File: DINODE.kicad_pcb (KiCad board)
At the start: 2 copper layers, 29 parts, among them J1 Barrel_Jack, J10 Conn_01x03_Male, J11 Conn_02x04_Odd_Even, J2 Conn_01x02_Male, J3 Conn_01x07, J4 Conn_01x16, J5 Conn_02x04_Odd_Even, J6 Conn_02x04_Odd_Even, J7 Conn_02x04_Odd_Even, J9 Conn_02x04_Odd_Even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

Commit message: Updated design
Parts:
- added J8: AVR-ISP-6, Connector_IDC:IDC-Header_2x03_P2.54mm_Horizontal, F.Cu at (141.6, 115.6)
- RV1, RV2: footprint Potentiometer_THT:Potentiometer_Piher_PT-15-V02_Vertical -> Potentiometer_THT:Potentiometer_Piher_PT-6-V_Vertical
- SW1: footprint Button_Switch_THT:SW_PUSH-12mm -> Button_Switch_THT:SW_PUSH_6mm_H5mm
- moved J5 95.6 mm to (102.9, 121.9), turned to 270 degrees
- moved C4 74.0 mm to (114.3, 62.2), turned to 270 degrees
- moved C3 70.8 mm to (105.4, 62.2), turned to 270 degrees
- moved J3 67.9 mm to (109.2, 121.3), turned to 90 degrees
- moved U2 66.9 mm to (123.2, 85.1)
- moved U3 64.4 mm to (124.5, 55.2)
- moved D1 61.0 mm to (128.3, 64.8)
- moved R1 61.0 mm to (114.9, 114.3), turned to 180 degrees
- moved RV1 60.9 mm to (101.0, 106.7)
- moved U1 60.1 mm to (108.0, 53.3)
- moved J10 59.0 mm to (135.9, 57.8), turned to 180 degrees
- moved J4 57.1 mm to (95.2, 106.7), turned to 180 degrees
- moved R2 55.4 mm to (104.1, 114.3), turned to 180 degrees
- moved J1 54.3 mm to (100.3, 53.3)
- moved J2 50.6 mm to (142.9, 56.5), turned to 180 degrees
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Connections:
- C4 pad 1: RESET -> +5V
- C6 pad 1: RESET -> +5V
- D1 pad 2: RESET -> +5V
- D2 pad 2: PC_7 -> PD_5
- J10 pad 3: RESET -> +5V
- J2 pad 2: RESET -> +5V
- J3 pad 1: RESET -> +5V
- J4 pad 15: RESET -> +5V
- J4 pad 2: RESET -> +5V
- J5 pad 1: ESP_RX -> GND
- J5 pad 2: +3V3 -> PD_0
- J5 pad 4: Net-(J5-Pad4) -> +3V3
- J5 pad 6: +3V3 -> Net-(J5-Pad6)
- J5 pad 7: GND -> ESP_RX
- J5 pad 8: PD_0 -> +3V3
- RV1 pad 3: RESET -> +5V
- RV2 pad 3: RESET -> +5V
- SW1 pad 2: RESET -> Net-(SW1-Pad2)
- U1 pad 3: RESET -> +5V
- U2 pad 17: RESET -> +5V
- U2 pad 38: RESET -> +5V
- U2 pad 4: RESET -> Net-(SW1-Pad2)
- U2 pad 5: RESET -> +5V
- U3 pad 3: RESET -> +5V
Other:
- board text added: "BY: Jack McLeans"
- board text added: "DINODE-AVR"
- board text added: "ESP8266"
- board text added: "GSM SIM800L V2.0"
- board text added: "LCD"
- board text added: "PA0"
- board text added: "PA1"
- board text added: "PA2"
- board text added: "PA3"
- board text added: "PA4"
- board text added: "PA5"
- board text added: "PA6"
- board text added: "PA7"
- board text added: "PB0"
- board text added: "PB1"
- board text added: "PB2"
- board text added: "PB3"
- board text added: "PB4"
- board text added: "PB5"
- board text added: "PB6"
- board text added: "PB7"
- board text added: "PC0"
- board text added: "PC1"
- board text added: "PC2"
- board text added: "PC3"
- board text added: "PC4"
- board text added: "PC5"
- board text added: "PC6"
- board text added: "PC7"
- board text added: "PD0"
- board text added: "PD1"
- board text added: "PD2"
- board text added: "PD3"
- board text added: "PD4"
- board text added: "PD5"
- board text added: "PD6"
- board text added: "PD7"

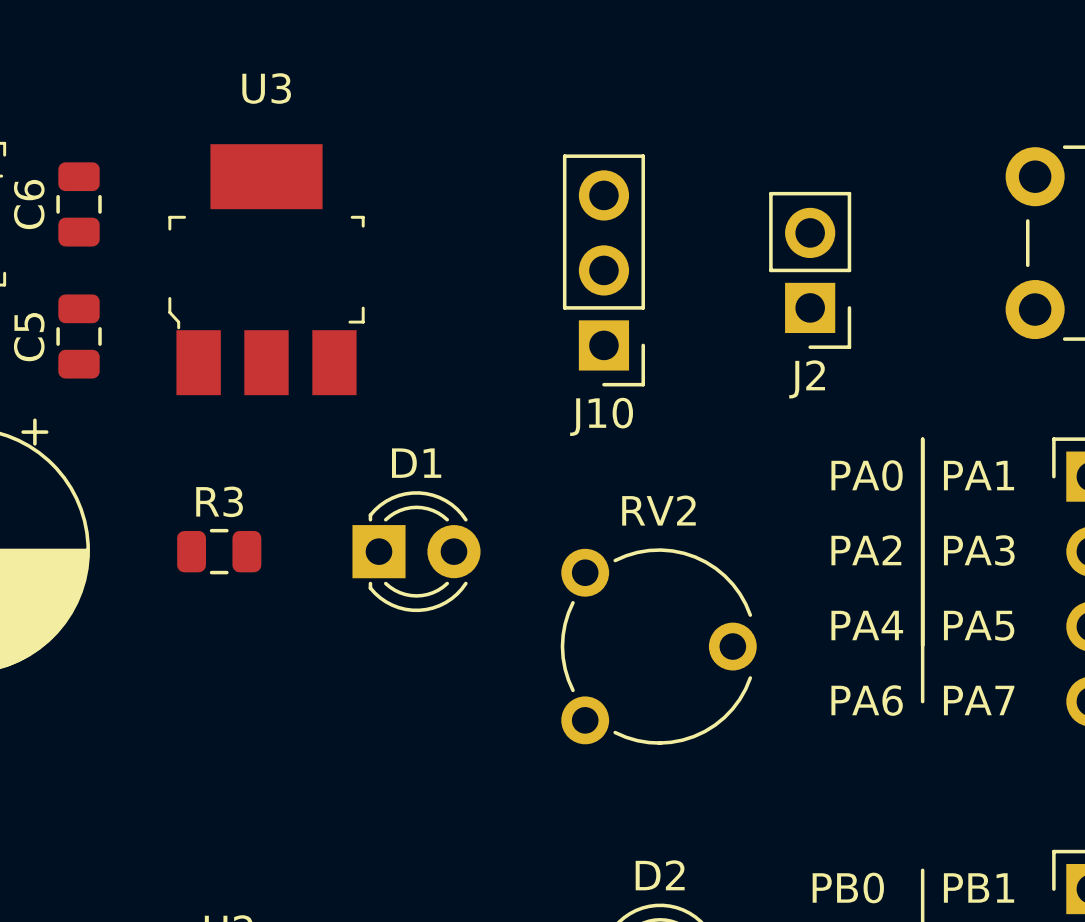
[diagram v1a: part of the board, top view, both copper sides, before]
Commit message: Updated power led position
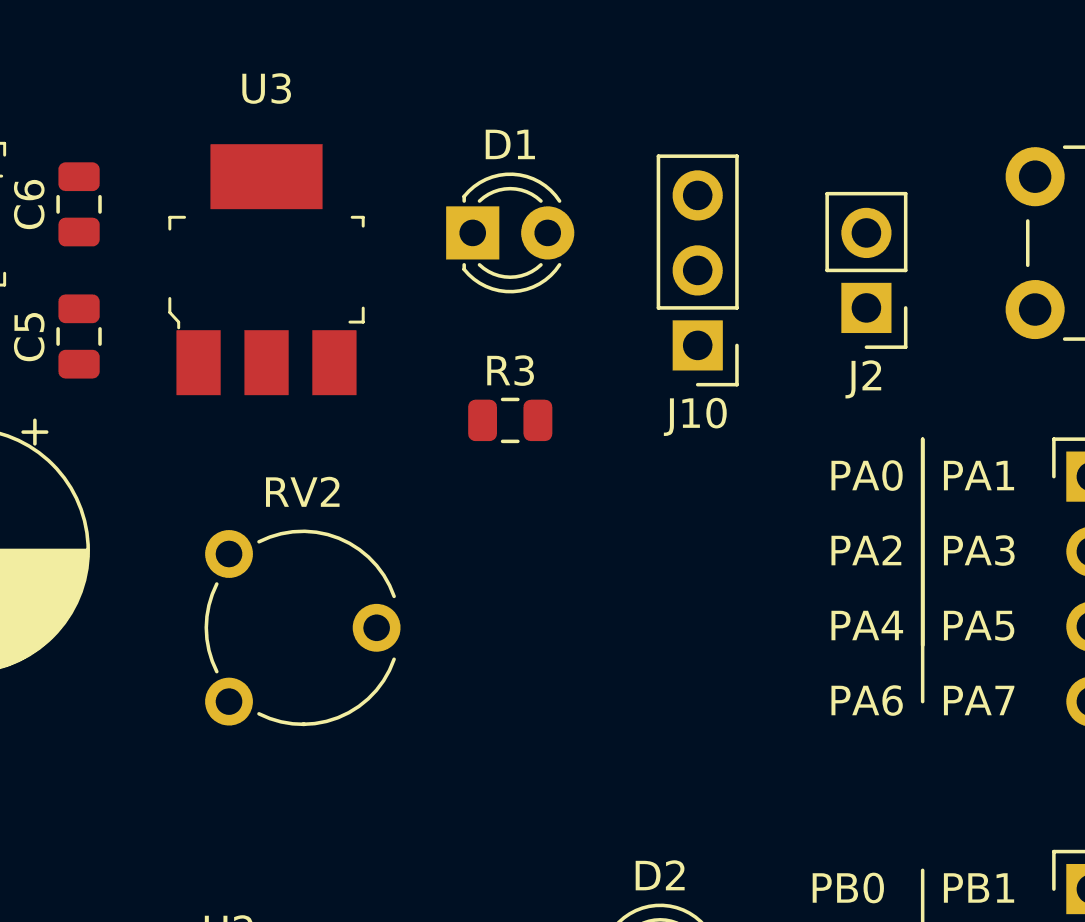
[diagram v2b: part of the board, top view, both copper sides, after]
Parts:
- moved RV2 12.1 mm to (123.2, 69.8)
- moved D1 11.3 mm to (131.4, 54.0)
- moved R3 10.8 mm to (132.7, 60.3)
- moved J10 3.18 mm to (139.1, 57.8)
- moved J2 1.91 mm to (144.8, 56.5)
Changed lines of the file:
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@@
   )
   (module LED_THT:LED_D3.0mm (layer F.Cu)
-    (at 128.27 64.77)
+    (at 131.445 53.975)
     (descr "LED, diameter 3.0mm, 2 pins")
     (tags "LED diameter 3.0mm 2 pins")
@@
   )
   (module Connector_PinHeader_2.54mm:PinHeader_1x02_P2.54mm_Vertical (layer F.Cu)
-    (at 142.875 56.515 180)
+    (at 144.78 56.515 180)
     (descr "Through hole straight pin header, 1x02, 2.54mm pitch, single row")
     (tags "Through hole pin header THT 1x02 2.54mm single row")
@@
   )
   (module Connector_PinHeader_2.54mm:PinHeader_1x03_P2.54mm_Vertical (layer F.Cu)
-    (at 135.89 57.785 180)
+    (at 139.065 57.785 180)
     (descr "Through hole straight pin header, 1x03, 2.54mm pitch, single row")
     (tags "Through hole pin header THT 1x03 2.54mm single row")
@@
   )
   (module Resistor_SMD:R_0805_2012Metric (layer F.Cu)
-    (at 122.8575 64.77)
+    (at 132.715 60.325)
     (descr "Resistor SMD 0805 (2012 Metric), square (rectangular) end terminal, IPC_7351 nominal, (Body size source: https://docs.google.com/spreadsheets/d/1BsfQQcO9C6DZCsRaXUlFlo91Tg2WpOkGARC1WS5S8t0/edit?usp=sharing), generated with kicad-footprint-generator")
     (tags resistor)
@@
   )
   (module Potentiometer_THT:Potentiometer_Piher_PT-6-V_Vertical (layer F.Cu)
-    (at 135.255 70.485)
+    (at 123.19 69.85)
     (descr "Potentiometer, vertical, Piher PT-6-V, http://www.piher-nacesa.com/pdf/11-PT6v03.pdf")
     (tags "Potentiometer vertical Piher PT-6-V")

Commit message: Started routing
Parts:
- added J12: Conn_01x03_Female, Connector_PinSocket_2.54mm:PinSocket_1x03_P2.54mm_Vertical, F.Cu at (153.7, 119.4)
- added J13: Conn_02x04_Odd_Even, Connector_PinSocket_2.54mm:PinSocket_2x04_P2.54mm_Vertical, F.Cu at (149.2, 118.1)
- moved J8 4.62 mm to (137.2, 114.3)
- moved R3 1.65 mm to (132.7, 58.7)
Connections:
- net Net-(C3-Pad1) renamed +12V
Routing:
- net GND: track 0.00 -> 260.7 mm, vias 0 -> 2
- net +5V: track 0.00 -> 128.6 mm, vias 0 -> 1
- net PA_0: track 0.00 -> 39.8 mm
- net +12V: track 0.00 -> 30.0 mm
- net ESP_RX: track 0.00 -> 23.5 mm
- net Net-(C2-Pad1): track 0.00 -> 20.7 mm
- net +3V3: track 0.00 -> 17.5 mm, vias 0 -> 1
- net Net-(D1-Pad1): track 0.00 -> 15.6 mm, vias 0 -> 1
- net Net-(C1-Pad1): track 0.00 -> 15.4 mm
- net PD_1: track 0.00 -> 9.94 mm
- net Net-(SW1-Pad2): track 0.00 -> 6.50 mm
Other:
- net class Default: trace_width 0.25 -> 0.3; via_dia 0.8 -> 0.65; via_drill 0.4 -> 0.35
- net class POWER AND GROUND added: clearance 0.2, trace_width 0.5, via_dia 0.65, via_drill 0.35

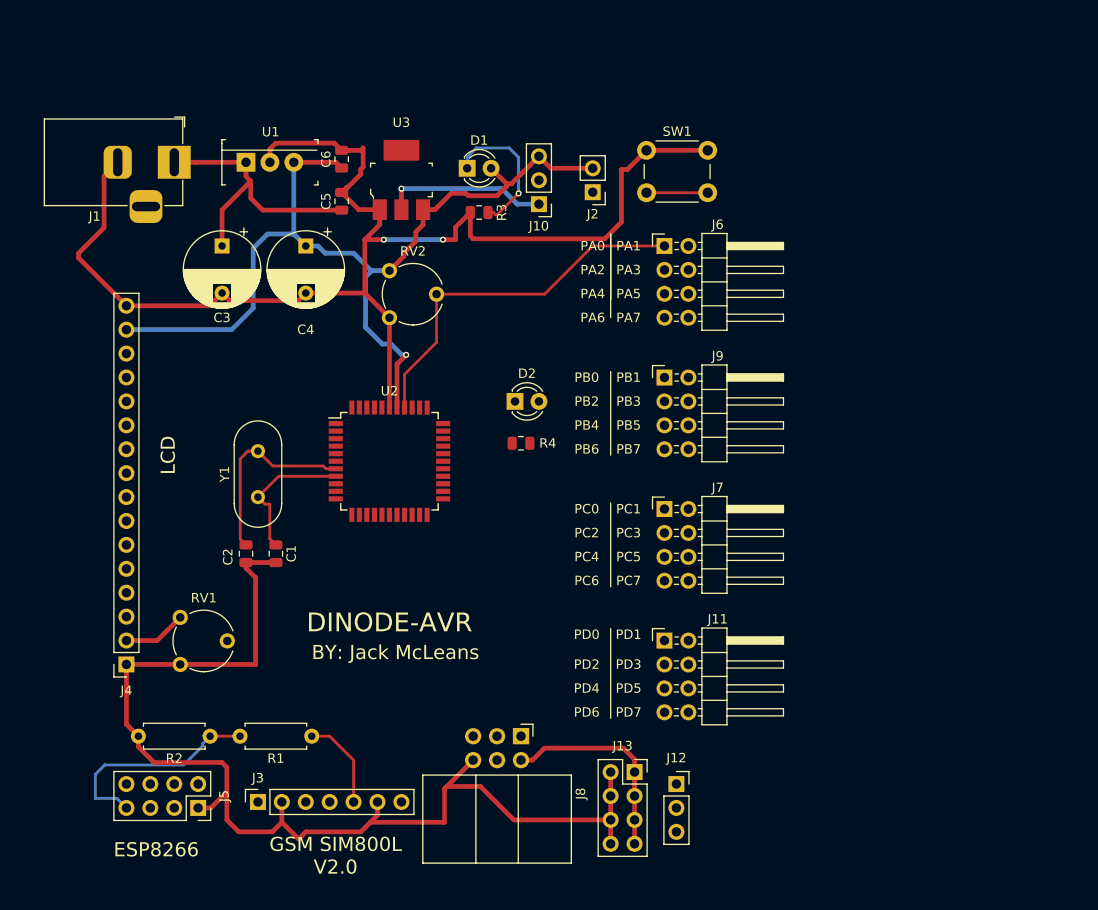
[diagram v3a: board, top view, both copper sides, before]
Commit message: Port C routing
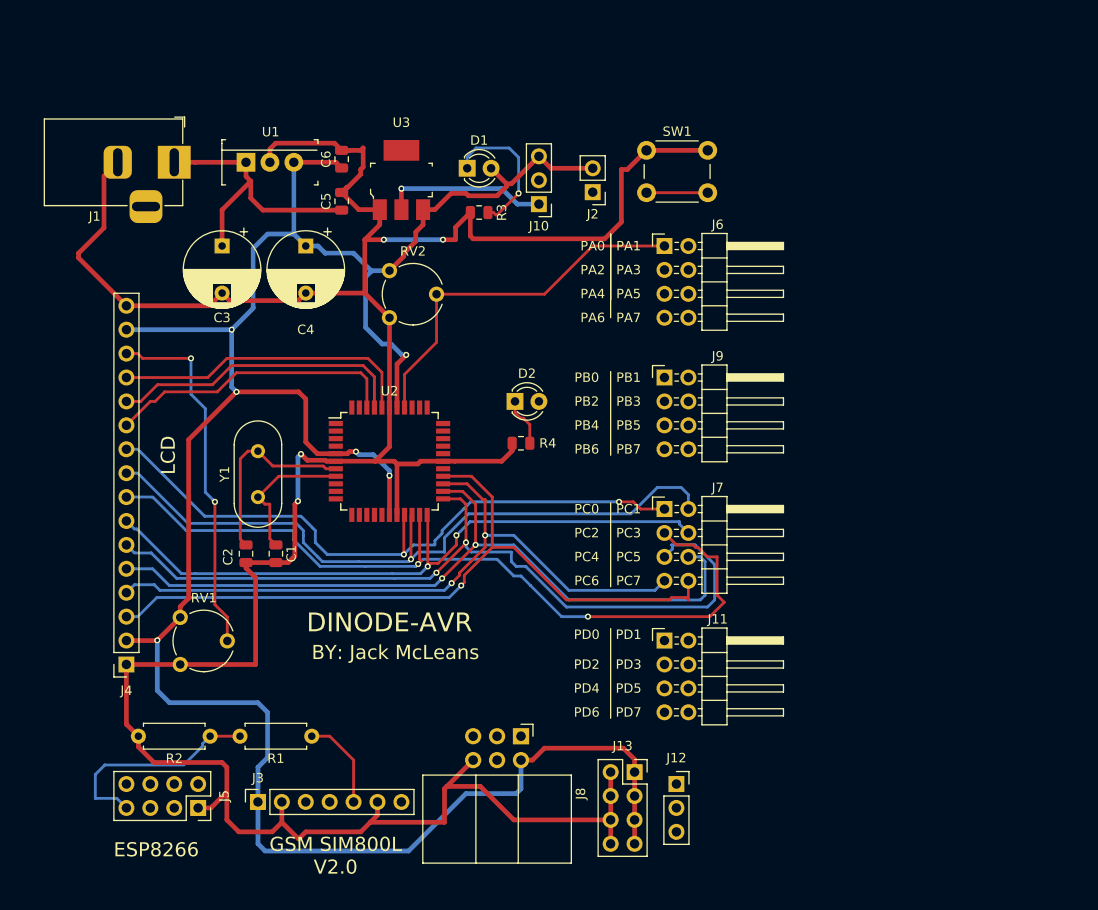
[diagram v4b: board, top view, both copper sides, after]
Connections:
- J9 pad 7: MOSI -> MISO
- SW1 pad 2: Net-(SW1-Pad2) -> RESET
- U2 pad 2: MOSI -> MISO
- U2 pad 4: Net-(SW1-Pad2) -> RESET
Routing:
- net +5V: track 128.6 -> 255.5 mm, vias 1 -> 6
- net PC_2: track 0.00 -> 87.8 mm, vias 0 -> 2
- net PC_4: track 0.00 -> 87.5 mm, vias 0 -> 2
- net PC_5: track 0.00 -> 80.5 mm, vias 0 -> 2
- net PC_7: track 0.00 -> 79.2 mm, vias 0 -> 1
- net PC_1: track 0.00 -> 75.1 mm, vias 0 -> 1
- net PC_6: track 0.00 -> 72.9 mm, vias 0 -> 2
- net PC_3: track 0.00 -> 71.0 mm, vias 0 -> 2
- net PC_0: track 0.00 -> 69.8 mm, vias 0 -> 2
- net GND: track 260.7 -> 310.0 mm, vias 2 -> 4
- net VO: track 0.00 -> 38.7 mm, vias 0 -> 2
- net PB_0: track 0.00 -> 32.3 mm
- net PB_1: track 0.00 -> 31.7 mm
- net PB_2: track 0.00 -> 31.2 mm
- net RESET: track 0.00 -> 6.50 mm
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
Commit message: Completed Routing
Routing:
- net +3V3: track 17.5 -> 185.4 mm, vias 1 -> 2
- net RESET: track 6.50 -> 145.0 mm, vias 0 -> 7
- net PB_7: track 0.00 -> 125.3 mm, vias 0 -> 2
- net PD_0: track 0.00 -> 122.6 mm, vias 0 -> 4
- net MISO: track 0.00 -> 111.6 mm, vias 0 -> 4
- net PD_5: track 0.00 -> 95.6 mm, vias 0 -> 1
- net MOSI: track 0.00 -> 79.9 mm, vias 0 -> 4
- net PD_1: track 9.94 -> 85.0 mm, vias 0 -> 2
- net PD_2: track 0.00 -> 61.0 mm, vias 0 -> 2
- net PD_3: track 0.00 -> 50.7 mm, vias 0 -> 1
- net PB_4: track 0.00 -> 50.4 mm, vias 0 -> 2
- net PD_7: track 0.00 -> 50.1 mm, vias 0 -> 1
- net PB_3: track 0.00 -> 47.2 mm, vias 0 -> 2
- net PD_4: track 0.00 -> 46.9 mm, vias 0 -> 1
- net PD_6: track 0.00 -> 45.8 mm, vias 0 -> 1
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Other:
- rule trace_min: 0.2 -> 0.25
- rule via_min_size: 0.4 -> 0.5
- board text added: "3V3"
- board text added: "5V"
- board text added: "AREF"
- board text added: "AVCC"
- board text added: "AVR-ISP-6"
- board text added: "GND"
- board text added: "LCD POT"
- board text added: "USER BUTTON"
- board text added: "USER LED"
- board text added: "USER POT"

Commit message: Addition of edge cuts
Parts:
- added H1: MountingHole, MountingHole:MountingHole_3.2mm_M3, F.Cu at (142.5, 46.2)
- added H2: MountingHole, MountingHole:MountingHole_3.2mm_M3, F.Cu at (89.9, 70.6)
- added H3: MountingHole, MountingHole:MountingHole_3.2mm_M3, F.Cu at (89.9, 112.0)
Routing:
- added copper zone on B.Cu, net GND
- added copper zone on F.Cu, net GND
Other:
- board outline added: 76.2 x 90.2 mm
- board text added: "RESET"
- board text removed: "USER BUTTON"
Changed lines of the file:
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@@
   (general
     (thickness 1.6)
-    (drawings 55)
+    (drawings 72)
     (tracks 1013)
     (zones 0)
-    (modules 32)
+    (modules 35)
     (nets 51)
   )
@@
     )
   )
+  (module MountingHole:MountingHole_3.2mm_M3 (layer F.Cu)
+    (at 142.494 46.228)
+    (descr "Mounting Hole 3.2mm, no annular, M3")
+    (tags "mounting hole 3.2mm no annular m3")
+    (attr virtual)
+    (fp_text reference H1 (at 4.953 0.254) (layer F.SilkS)
+      (effects (font (size 1 1) (thickness 0.15)))
+    )
+    (fp_text value MountingHole (at 0 4.2) (layer F.Fab)
+      (effects (font (size 1 1) (thickness 0.15)))
+    )
+    (fp_text user %R (at 0.3 0) (layer F.Fab)
+      (effects (font (size 1 1) (thickness 0.15)))
+    )
+    (fp_circle (center 0 0) (end 3.2 0) (layer Cmts.User) (width 0.15))
+    (fp_circle (center 0 0) (end 3.45 0) (layer F.CrtYd) (width 0.05))
+    (pad 1 np_thru_hole circle (at 0 0) (size 3.2 3.2) (drill 3.2) (layers *.Cu *.Mask))
+  )
+  (module MountingHole:MountingHole_3.2mm_M3 (layer F.Cu)
+    (at 89.916 70.612)
+    (descr "Mounting Hole 3.2mm, no annular, M3")
+    (tags "mounting hole 3.2mm no annular m3")
+    (attr virtual)
+    (fp_text reference H2 (at 0 -4.2) (layer F.SilkS)
+      (effects (font (size 1 1) (thickness 0.15)))
+    )
+    (fp_text value MountingHole (at 0 4.2) (layer F.Fab)
+      (effects (font (size 1 1) (thickness 0.15)))
+    )
+    (fp_circle (center 0 0) (end 3.45 0) (layer F.CrtYd) (width 0.05))
+    (fp_circle (center 0 0) (end 3.2 0) (layer Cmts.User) (width 0.15))
+    (fp_text user %R (at 0.3 0) (layer F.Fab)
+      (effects (font (size 1 1) (thickness 0.15)))
+    )
+    (pad 1 np_thru_hole circle (at 0 0) (size 3.2 3.2) (drill 3.2) (layers *.Cu *.Mask))
+  )
+  (module MountingHole:MountingHole_3.2mm_M3 (layer F.Cu)
+    (at 89.916 112.014)
+    (descr "Mounting Hole 3.2mm, no annular, M3")
+    (tags "mounting hole 3.2mm no annular m3")
+    (attr virtual)
+    (fp_text reference H3 (at 4.699 0.381) (layer F.SilkS)
+      (effects (font (size 1 1) (thickness 0.15)))
+    )
+    (fp_text value MountingHole (at 0 4.2) (layer F.Fab)
+      (effects (font (size 1 1) (thickness 0.15)))
+    )
+    (fp_text user %R (at 0.3 0) (layer F.Fab)
+      (effects (font (size 1 1) (thickness 0.15)))
+    )
+    (fp_circle (center 0 0) (end 3.2 0) (layer Cmts.User) (width 0.15))
+    (fp_circle (center 0 0) (end 3.45 0) (layer F.CrtYd) (width 0.05))
+    (pad 1 np_thru_hole circle (at 0 0) (size 3.2 3.2) (drill 3.2) (layers *.Cu *.Mask))
+  )
+  (gr_line (start 137.16 43.18) (end 111.76 43.18) (layer Edge.Cuts) (width 0.05))
+  (gr_line (start 137.16 46.99) (end 137.16 43.18) (layer Edge.Cuts) (width 0.05))
+  (gr_line (start 111.76 46.99) (end 137.16 46.99) (layer Edge.Cuts) (width 0.05))
+  (gr_line (start 111.76 43.18) (end 111.76 46.99) (layer Edge.Cuts) (width 0.05))
+  (gr_line (start 161.29 45.72) (end 161.29 48.26) (layer Edge.Cuts) (width 0.05))
+  (gr_line (start 148.59 45.72) (end 161.29 45.72) (layer Edge.Cuts) (width 0.05))
+  (gr_line (start 138.303 39.37) (end 148.59 45.72) (layer Edge.Cuts) (width 0.05))
+  (gr_line (start 136.017 39.37) (end 138.303 39.37) (layer Edge.Cuts) (width 0.05))
+  (gr_line (start 111.76 39.37) (end 136.017 39.37) (layer Edge.Cuts) (width 0.05))
+  (gr_line (start 101.473 45.72) (end 111.76 39.37) (layer Edge.Cuts) (width 0.05))
+  (gr_line (start 86.995 45.72) (end 101.473 45.72) (layer Edge.Cuts) (width 0.05))
+  (gr_line (start 85.09 45.72) (end 86.995 45.72) (layer Edge.Cuts) (width 0.05))
+  (gr_line (start 130.81 129.54) (end 161.29 129.54) (layer Edge.Cuts) (width 0.05))
+  (gr_line (start 161.29 129.54) (end 161.29 48.26) (layer Edge.Cuts) (width 0.05))
+  (gr_line (start 85.09 129.54) (end 90.17 129.54) (layer Edge.Cuts) (width 0.05))
+  (gr_line (start 85.09 45.72) (end 85.09 129.54) (layer Edge.Cuts) (width 0.05))
+  (gr_line (start 90.17 129.54) (end 130.81 129.54) (layer Edge.Cuts) (width 0.05))
   (gr_text "USER LED" (at 134.366 78.994 90) (layer F.SilkS)
     (effects (font (size 1 1) (thickness 0.15)))
@@
     (effects (font (size 1 1) (thickness 0.15)))
   )
-  (gr_text "USER BUTTON" (at 153.924 58.674) (layer F.SilkS)
+  (gr_text RESET (at 153.924 58.674) (layer F.SilkS)
     (effects (font (size 1 1) (thickness 0.15)))
   )
@@
   (segment (start 108.458 57.15) (end 109.728 58.42) (width 0.5) (layer F.Cu) (net 50))
   (segment (start 109.728 58.42) (end 118.11 58.42) (width 0.5) (layer F.Cu) (net 50))
+  (zone (net 1) (net_name GND) (layer F.Cu) (hatch edge 0.508)
+    (connect_pads (clearance 0.508))
+    (min_thickness 0.254)
+    (fill yes (arc_segments 32) (thermal_gap 0.508) (thermal_bridge_width 0.508))
+    (polygon
+      (pts
+        (xy 83.947 130.81) (xy 162.433 130.81) (xy 162.56 44.45) (xy 148.463 44.45) (xy 138.303 38.1)
+        (xy 111.633 38.1) (xy 101.6 44.45) (xy 83.82 44.323)
+      )
+    )
+  )
+  (zone (net 1) (net_name GND) (layer B.Cu) (hatch edge 0.508)
+    (connect_pads (clearance 0.508))
+    (min_thickness 0.254)
+    (fill yes (arc_segments 32) (thermal_gap 0.508) (thermal_bridge_width 0.508))
+    (polygon
+      (pts
+        (xy 83.947 130.81) (xy 162.433 130.81) (xy 162.56 44.45) (xy 148.463 44.45) (xy 138.303 38.1)
+        (xy 111.633 38.1) (xy 101.6 44.45) (xy 83.82 44.323)
+      )
+    )
+  )
 )
